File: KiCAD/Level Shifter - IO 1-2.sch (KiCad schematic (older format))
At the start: 143 parts, among them Q10 DMN63D8LDW, Q3 MMBT3904, Q4 MMBT3906, Q5 DMG1029SV, Q6 MMBT3904, Q7 MMBT3906, Q8 DMG1029SV, Q9 MMBT3904, U10 PI5A3157, U11 LM7171, U12 LM7171, U13 LM7171, U14 PI5A3157, U15 LM7171, U16 LM7171, U17 DG448DV, U18 DG448DV, U5 MCP4728A0, U6 NCV20074, U7 TS3011, U8 MCP4725A0, U9 TS3011

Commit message: Add power changeover circuit, fix minor issues
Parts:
- C55, C56, C59: value 0 -> C
- C62, C63, C68, C69, C70, C71: value 10u -> 0.1u
- R77, R78, R91: value 0 -> R
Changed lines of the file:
@@
 Sheet 4 10
 Title "LEVEL SHIFTER SUBSYSTEM - I/O PINS 1 & 2"
-Date "2020-02-03"
+Date "2020-02-04"
 Rev "A"
 Comp "THE UNIVERSITY OF AKRON"
@@
 P 10900 7850
 F 0 "C68" H 11015 7896 50  0000 L CNN
-F 1 "10u" H 11015 7805 50  0000 L CNN
+F 1 "0.1u" H 11015 7805 50  0000 L CNN
 F 2 "" H 10938 7700 50  0001 C CNN
 F 3 "~" H 10900 7850 50  0001 C CNN
@@
 P 10900 8250
 F 0 "C69" H 11015 8296 50  0000 L CNN
-F 1 "10u" H 11015 8205 50  0000 L CNN
+F 1 "0.1u" H 11015 8205 50  0000 L CNN
 F 2 "" H 10938 8100 50  0001 C CNN
 F 3 "~" H 10900 8250 50  0001 C CNN
@@
 P 8350 6400
 F 0 "C62" H 8465 6446 50  0000 L CNN
-F 1 "10u" H 8465 6355 50  0000 L CNN
+F 1 "0.1u" H 8465 6355 50  0000 L CNN
 F 2 "" H 8388 6250 50  0001 C CNN
 F 3 "~" H 8350 6400 50  0001 C CNN
@@
 P 8350 6800
 F 0 "C63" H 8465 6846 50  0000 L CNN
-F 1 "10u" H 8465 6755 50  0000 L CNN
+F 1 "0.1u" H 8465 6755 50  0000 L CNN
 F 2 "" H 8388 6650 50  0001 C CNN
 F 3 "~" H 8350 6800 50  0001 C CNN
@@
 P 10950 1500
 F 0 "C70" H 11065 1546 50  0000 L CNN
-F 1 "10u" H 11065 1455 50  0000 L CNN
+F 1 "0.1u" H 11065 1455 50  0000 L CNN
 F 2 "" H 10988 1350 50  0001 C CNN
 F 3 "~" H 10950 1500 50  0001 C CNN
@@
 P 10950 1900
 F 0 "C71" H 11065 1946 50  0000 L CNN
-F 1 "10u" H 11065 1855 50  0000 L CNN
+F 1 "0.1u" H 11065 1855 50  0000 L CNN
 F 2 "" H 10988 1750 50  0001 C CNN
 F 3 "~" H 10950 1900 50  0001 C CNN
@@
 CMP1-
 $Comp
-L Device:R R77
-U 1 1 5EEE98DF
-P 6050 3500
-F 0 "R77" V 5950 3500 50  0000 C CNN
-F 1 "0" V 6050 3500 50  0001 C CNN
-F 2 "" V 5980 3500 50  0001 C CNN
-F 3 "~" H 6050 3500 50  0001 C CNN
-F 4 "DO NOT POP" V 6150 3500 39  0000 C CNN "Depop"
-	1    6050 3500
-	0    -1   1    0
-$EndComp
-$Comp
 L Device:C C55
 U 1 1 5FC14A98
 P 6450 3500
 F 0 "C55" V 6300 3500 50  0000 C CNN
-F 1 "0" V 6300 3600 50  0001 C CNN
+F 1 "C" V 6300 3600 50  0001 C CNN
 F 2 "" H 6488 3350 50  0001 C CNN
 F 3 "~" H 6450 3500 50  0001 C CNN
@@
 P 6250 6750
 F 0 "R78" V 6150 6750 50  0000 C CNN
-F 1 "0" V 6250 6750 50  0001 C CNN
+F 1 "R" V 6250 6750 50  0001 C CNN
 F 2 "" V 6180 6750 50  0001 C CNN
 F 3 "~" H 6250 6750 50  0001 C CNN
@@
 P 6650 6750
 F 0 "C56" V 6500 6750 50  0000 C CNN
-F 1 "0" V 6500 6850 50  0001 C CNN
+F 1 "C" V 6500 6850 50  0001 C CNN
 F 2 "" H 6688 6600 50  0001 C CNN
 F 3 "~" H 6650 6750 50  0001 C CNN
@@
 P 7850 7900
 F 0 "R91" V 7750 7900 50  0000 C CNN
-F 1 "0" V 7850 7900 50  0001 C CNN
+F 1 "R" V 7850 7900 50  0001 C CNN
 F 2 "" V 7780 7900 50  0001 C CNN
 F 3 "~" H 7850 7900 50  0001 C CNN
@@
 P 8250 7900
 F 0 "C59" V 8100 7900 50  0000 C CNN
-F 1 "0" V 8100 8000 50  0001 C CNN
+F 1 "C" V 8100 8000 50  0001 C CNN
 F 2 "" H 8288 7750 50  0001 C CNN
 F 3 "~" H 8250 7900 50  0001 C CNN
@@
 Wire Wire Line
 	15050 4850 15100 4850
+$Comp
+L Device:R R77
+U 1 1 5EEE98DF
+P 6050 3500
+F 0 "R77" V 5950 3500 50  0000 C CNN
+F 1 "R" V 6050 3500 50  0001 C CNN
+F 2 "" V 5980 3500 50  0001 C CNN
+F 3 "~" H 6050 3500 50  0001 C CNN
+F 4 "DO NOT POP" V 6150 3500 39  0000 C CNN "Depop"
+	1    6050 3500
+	0    -1   1    0
+$EndComp
 $EndSCHEMATC

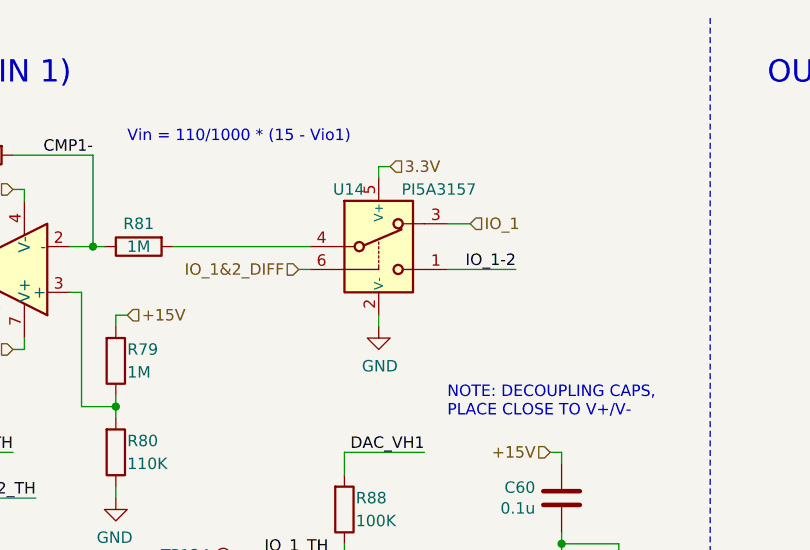
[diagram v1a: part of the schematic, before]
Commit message: Replace switches U14 and U31 with higher voltage part
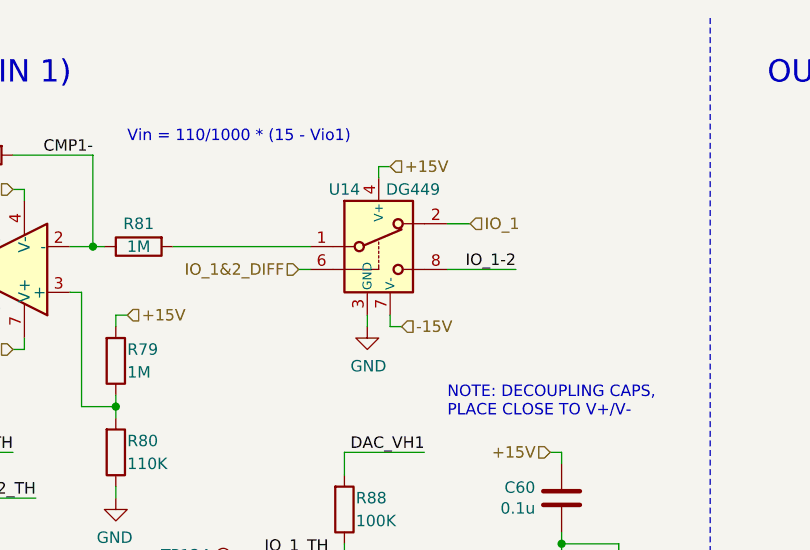
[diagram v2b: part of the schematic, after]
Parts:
- removed U14: PI5A3157, Package_TO_SOT_SMD:SOT-363_SC-70-6, symbol io-master:PI5A3157
- added U14: DG449, Package_TO_SOT_SMD:SOT-23-8, symbol io-master:DG449
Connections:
- net +15V: now also U14.4 (V+)
- net -15V: now also U14.7 (V-)
- net CMP+: now also U14.8
- net GND: now also U14.3 (GND)
- net IO_1: now also U14.2
- net IO_1&2_DIFF: now also U14.6
- net at R81.2: now also U14.1
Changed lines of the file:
@@
 Wire Wire Line
 	5300 2800 5300 2850
-$Comp
-L io-master:PI5A3157 U14
-U 1 1 5FC14A81
-P 7550 1400
-F 0 "U14" H 7350 1550 50  0000 L CNN
-F 1 "PI5A3157" H 7650 1550 50  0000 L CNN
-F 2 "Package_TO_SOT_SMD:SOT-363_SC-70-6" H 7550 1100 50  0001 C CNN
-F 3 "https://www.diodes.com/assets/Datasheets/PI5A3157.pdf" H 7550 1200 50  0001 C CNN
-	1    7550 1400
-	1    0    0    -1
-$EndComp
 Wire Wire Line
 	7200 1600 7250 1600
@@
 L power:GND #PWR067
 U 1 1 5FC14A82
-P 7550 1850
-F 0 "#PWR067" H 7550 1600 50  0001 C CNN
-F 1 "GND" H 7555 1677 50  0000 C CNN
-F 2 "" H 7550 1850 50  0001 C CNN
-F 3 "" H 7550 1850 50  0001 C CNN
-	1    7550 1850
-	1    0    0    -1
-$EndComp
-Text HLabel 7600 1150 2    50   Input ~ 0
-3.3V
+P 7500 1850
+F 0 "#PWR067" H 7500 1600 50  0001 C CNN
+F 1 "GND" H 7505 1677 50  0000 C CNN
+F 2 "" H 7500 1850 50  0001 C CNN
+F 3 "" H 7500 1850 50  0001 C CNN
+	1    7500 1850
+	1    0    0    -1
+$EndComp
 Wire Wire Line
 	7600 1150 7550 1150
@@
 	7550 1150 7550 1200
 Wire Wire Line
-	7550 1800 7550 1850
+	7500 1800 7500 1850
 Text HLabel 7200 1600 0    50   Input ~ 0
 IO_1&2_DIFF
@@
 	0    -1   1    0
 $EndComp
+$Comp
+L io-master:DG449 U14
+U 1 1 5E3F032D
+P 7550 1400
+F 0 "U14" H 7400 1550 50  0000 C CNN
+F 1 "DG449" H 7700 1550 50  0000 C CNN
+F 2 "Package_TO_SOT_SMD:SOT-23-8" H 7550 1100 50  0001 C CNN
+F 3 "http://www.vishay.com/docs/73897/dg449.pdf" H 7550 1200 50  0001 C CNN
+	1    7550 1400
+	1    0    0    -1
+$EndComp
+Text HLabel 7600 1150 2    50   Input ~ 0
++15V
+Text HLabel 7650 1850 2    50   Input ~ 0
+-15V
+Wire Wire Line
+	7650 1850 7600 1850
+Wire Wire Line
+	7600 1850 7600 1800
 $EndSCHEMATC

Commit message: Assign footprints, fix minor schematic issues
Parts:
- C47, C48, C49, C50, C51, C52, C53, C54, C55, C56, C57, C58, C59, C60, C61, C62, C63, C68, C69, C70, C71, C72: footprint (none) -> Capacitor_SMD:C_0603_1608Metric
- C64, C65, C66, C67: footprint (none) -> Capacitor_SMD:C_0805_2012Metric
- D14, D15: footprint (none) -> Diode_SMD:D_SOD-323
- Q3, Q4, Q6, Q7, Q9: footprint Package_TO_SOT_SMD:SOT-23 -> Package_TO_SOT_SMD:SOT-323_SC-70
- R100, R101, R102, R103, R104, R105, R106, R107, R108, R109, R110, R111, R112, R113, R114, R115, R116, R117, R118, R50, R51, R52, R53, R54, R55, R56, R57, R58, R59, R60, R61, R62, R63, R64, R65, R66, R67, R68, R69, R70, R71, R72, R73, R74, R75, R76, R77, R78, R79, R80, R81, R82, R83, R84, R85, R86, R87, R88, R89, R90, R91, R92, R93, R94, R95, R96, R97, R98, R99: footprint (none) -> Resistor_SMD:R_0603_1608Metric
- R119, R120, R121, R122: footprint (none) -> Resistor_SMD:R_0805_2012Metric
- TP112: value TestPoint -> DVH1; footprint (none) -> TestPoint:TestPoint_Pad_D1.0mm
- TP113: value TestPoint -> DVL1; footprint (none) -> TestPoint:TestPoint_Pad_D1.0mm
- TP114: value TestPoint -> DVH2; footprint (none) -> TestPoint:TestPoint_Pad_D1.0mm
- TP115: value TestPoint -> DVL2; footprint (none) -> TestPoint:TestPoint_Pad_D1.0mm
- TP116: value TestPoint -> VH1; footprint (none) -> TestPoint:TestPoint_Pad_D1.0mm
- TP117: value TestPoint -> VL1; footprint (none) -> TestPoint:TestPoint_Pad_D1.0mm
- TP118: value TestPoint -> VH2; footprint (none) -> TestPoint:TestPoint_Pad_D1.0mm
- TP119: value TestPoint -> VL2; footprint (none) -> TestPoint:TestPoint_Pad_D1.0mm
- TP120, TP121, TP125, TP126, TP127, TP128, TP129, TP130, TP131: footprint (none) -> TestPoint:TestPoint_Pad_D1.0mm
- TP122: value TestPoint -> TH12; footprint (none) -> TestPoint:TestPoint_Pad_D1.0mm
- TP123: value TestPoint -> 1-2; footprint (none) -> TestPoint:TestPoint_Pad_D1.0mm
- TP124: value TestPoint -> TH1; footprint (none) -> TestPoint:TestPoint_Pad_D1.0mm

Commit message: Add C18 and C21 0.1u decoupling caps, fix minor issues
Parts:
- added C18: 0.1u, Capacitor_SMD:C_0603_1608Metric, symbol Device:C
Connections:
- net +15V: now also C54.1
- net -15V: now also C18.2
- net 3.3V: no longer C54.1
- net GND: now also C18.1
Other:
- moved on the sheet: C50, C52, C60, C61
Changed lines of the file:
@@
 Sheet 4 10
 Title "LEVEL SHIFTER SUBSYSTEM - I/O PINS 1 & 2"
-Date "2020-02-07"
+Date "2020-02-10"
 Rev "A"
 Comp "THE UNIVERSITY OF AKRON"
@@
 L Device:C C50
 U 1 1 60160A18
-P 4000 3100
-F 0 "C50" H 4115 3146 50  0000 L CNN
-F 1 "0.1u" H 4115 3055 50  0000 L CNN
-F 2 "Capacitor_SMD:C_0603_1608Metric" H 4038 2950 50  0001 C CNN
-F 3 "~" H 4000 3100 50  0001 C CNN
-	1    4000 3100
+P 4100 3100
+F 0 "C50" H 4215 3146 50  0000 L CNN
+F 1 "0.1u" H 4215 3055 50  0000 L CNN
+F 2 "Capacitor_SMD:C_0603_1608Metric" H 4138 2950 50  0001 C CNN
+F 3 "~" H 4100 3100 50  0001 C CNN
+	1    4100 3100
 	1    0    0    -1
 $EndComp
@@
 L power:GND #PWR057
 U 1 1 60160A22
-P 4000 3350
-F 0 "#PWR057" H 4000 3100 50  0001 C CNN
-F 1 "GND" H 4005 3177 50  0000 C CNN
-F 2 "" H 4000 3350 50  0001 C CNN
-F 3 "" H 4000 3350 50  0001 C CNN
-	1    4000 3350
+P 4100 3350
+F 0 "#PWR057" H 4100 3100 50  0001 C CNN
+F 1 "GND" H 4105 3177 50  0000 C CNN
+F 2 "" H 4100 3350 50  0001 C CNN
+F 3 "" H 4100 3350 50  0001 C CNN
+	1    4100 3350
 	1    0    0    -1
 $EndComp
 Wire Wire Line
-	4000 3350 4000 3300
+	4100 3350 4100 3300
 Wire Wire Line
-	4000 2900 4000 2950
+	4100 2900 4100 2950
 Text Notes 3850 3800 0    50   ~ 0
 NOTE: DECOUPLING CAPS,\nPLACE CLOSE TO V+
-Text HLabel 3950 2900 0    50   Input ~ 0
+Text HLabel 4050 2900 0    50   Input ~ 0
 3.3V
 Wire Wire Line
-	3950 2900 4000 2900
+	4050 2900 4100 2900
 $Comp
 L Device:C C60
 U 1 1 601A4E02
-P 8350 2600
-F 0 "C60" H 8465 2646 50  0000 L CNN
-F 1 "0.1u" H 8465 2555 50  0000 L CNN
-F 2 "Capacitor_SMD:C_0603_1608Metric" H 8388 2450 50  0001 C CNN
-F 3 "~" H 8350 2600 50  0001 C CNN
-	1    8350 2600
+P 8200 2600
+F 0 "C60" H 8315 2646 50  0000 L CNN
+F 1 "0.1u" H 8315 2555 50  0000 L CNN
+F 2 "Capacitor_SMD:C_0603_1608Metric" H 8238 2450 50  0001 C CNN
+F 3 "~" H 8200 2600 50  0001 C CNN
+	1    8200 2600
 	-1   0    0    -1
 $EndComp
@@
 L power:GND #PWR071
 U 1 1 601A4E0C
-P 8600 2850
-F 0 "#PWR071" H 8600 2600 50  0001 C CNN
-F 1 "GND" H 8605 2677 50  0000 C CNN
-F 2 "" H 8600 2850 50  0001 C CNN
-F 3 "" H 8600 2850 50  0001 C CNN
-	1    8600 2850
+P 8800 2850
+F 0 "#PWR071" H 8800 2600 50  0001 C CNN
+F 1 "GND" H 8805 2677 50  0000 C CNN
+F 2 "" H 8800 2850 50  0001 C CNN
+F 3 "" H 8800 2850 50  0001 C CNN
+	1    8800 2850
 	1    0    0    -1
 $EndComp
 Wire Wire Line
-	8350 2400 8350 2450
+	8200 2400 8200 2450
 Text Notes 7850 2250 0    50   ~ 0
 NOTE: DECOUPLING CAPS,\nPLACE CLOSE TO V+/V-
 Wire Wire Line
-	8300 2400 8350 2400
+	8150 2400 8200 2400
 $Comp
 L Device:C C61
 U 1 1 601A4E19
-P 8350 3000
-F 0 "C61" H 8465 3046 50  0000 L CNN
-F 1 "0.1u" H 8465 2955 50  0000 L CNN
-F 2 "Capacitor_SMD:C_0603_1608Metric" H 8388 2850 50  0001 C CNN
-F 3 "~" H 8350 3000 50  0001 C CNN
-	1    8350 3000
+P 8200 3000
+F 0 "C61" H 8315 3046 50  0000 L CNN
+F 1 "0.1u" H 8315 2955 50  0000 L CNN
+F 2 "Capacitor_SMD:C_0603_1608Metric" H 8238 2850 50  0001 C CNN
+F 3 "~" H 8200 3000 50  0001 C CNN
+	1    8200 3000
 	-1   0    0    -1
 $EndComp
 Wire Wire Line
-	8350 2750 8350 2800
+	8200 2750 8200 2800
 Wire Wire Line
-	8300 3200 8350 3200
+	8150 3200 8200 3200
 Wire Wire Line
-	8350 3200 8350 3150
-Connection ~ 8350 2800
+	8200 3200 8200 3150
+Connection ~ 8200 2800
 Wire Wire Line
-	8350 2800 8350 2850
-Wire Wire Line
-	8600 2800 8600 2850
-Wire Wire Line
-	8350 2800 8600 2800
-Text HLabel 8300 2400 0    50   Input ~ 0
+	8200 2800 8200 2850
+Text HLabel 8150 2400 0    50   Input ~ 0
 +15V
-Text HLabel 8300 3200 0    50   Input ~ 0
+Text HLabel 8150 3200 0    50   Input ~ 0
 -15V
 $Comp
@@
 L Device:C C52
 U 1 1 5FC14ADB
-P 4400 3100
-F 0 "C52" H 4515 3146 50  0000 L CNN
-F 1 "0.1u" H 4515 3055 50  0000 L CNN
-F 2 "Capacitor_SMD:C_0603_1608Metric" H 4438 2950 50  0001 C CNN
-F 3 "~" H 4400 3100 50  0001 C CNN
-	1    4400 3100
+P 4500 3100
+F 0 "C52" H 4615 3146 50  0000 L CNN
+F 1 "0.1u" H 4615 3055 50  0000 L CNN
+F 2 "Capacitor_SMD:C_0603_1608Metric" H 4538 2950 50  0001 C CNN
+F 3 "~" H 4500 3100 50  0001 C CNN
+	1    4500 3100
 	1    0    0    -1
 $EndComp
-$Comp
-L Device:C C54
-U 1 1 5FC14ADC
-P 4800 3100
-F 0 "C54" H 4915 3146 50  0000 L CNN
-F 1 "0.1u" H 4915 3055 50  0000 L CNN
-F 2 "Capacitor_SMD:C_0603_1608Metric" H 4838 2950 50  0001 C CNN
-F 3 "~" H 4800 3100 50  0001 C CNN
-	1    4800 3100
-	1    0    0    -1
-$EndComp
-Wire Wire Line
-	4000 2900 4400 2900
 Wire Wire Line
-	4800 2900 4800 2950
-Connection ~ 4000 2900
+	4100 2900 4500 2900
+Connection ~ 4100 2900
 Wire Wire Line
-	4400 2950 4400 2900
-Connection ~ 4400 2900
+	4500 2950 4500 2900
 Wire Wire Line
-	4400 2900 4800 2900
+	4100 3300 4500 3300
 Wire Wire Line
-	4000 3300 4400 3300
+	4500 3300 4500 3250
+Connection ~ 4100 3300
 Wire Wire Line
-	4400 3300 4400 3250
-Connection ~ 4000 3300
-Wire Wire Line
-	4000 3300 4000 3250
-Wire Wire Line
-	4400 3300 4800 3300
-Wire Wire Line
-	4800 3300 4800 3250
-Connection ~ 4400 3300
+	4100 3300 4100 3250
 Text Notes 4700 6100 0    50   ~ 0
 THRESHOLD = 1000/110 * (1.65V - Vdac)
@@
 Wire Wire Line
 	7600 1850 7600 1800
+$Comp
+L Device:C C54
+U 1 1 5FA79B18
+P 8600 2600
+F 0 "C54" H 8715 2646 50  0000 L CNN
+F 1 "0.1u" H 8715 2555 50  0000 L CNN
+F 2 "Capacitor_SMD:C_0603_1608Metric" H 8638 2450 50  0001 C CNN
+F 3 "~" H 8600 2600 50  0001 C CNN
+	1    8600 2600
+	-1   0    0    -1
+$EndComp
+$Comp
+L Device:C C18
+U 1 1 5FA7A360
+P 8600 3000
+F 0 "C18" H 8715 3046 50  0000 L CNN
+F 1 "0.1u" H 8715 2955 50  0000 L CNN
+F 2 "Capacitor_SMD:C_0603_1608Metric" H 8638 2850 50  0001 C CNN
+F 3 "~" H 8600 3000 50  0001 C CNN
+	1    8600 3000
+	-1   0    0    -1
+$EndComp
+Wire Wire Line
+	8800 2800 8800 2850
+Wire Wire Line
+	8200 2800 8600 2800
+Wire Wire Line
+	8600 2850 8600 2800
+Connection ~ 8600 2800
+Wire Wire Line
+	8600 2800 8800 2800
+Wire Wire Line
+	8600 2800 8600 2750
+Wire Wire Line
+	8200 2400 8600 2400
+Wire Wire Line
+	8600 2400 8600 2450
+Connection ~ 8200 2400
+Wire Wire Line
+	8200 3200 8600 3200
+Wire Wire Line
+	8600 3200 8600 3150
+Connection ~ 8200 3200
 $EndSCHEMATC
